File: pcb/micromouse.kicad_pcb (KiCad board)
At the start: 2 copper layers, 46 x 84 mm, 64 parts, among them J1 PINHD_1x6_Female, J10 B2B-PH-K-S, J11 B2B-PH-K-S, J12 PINHD_1x5_Female, J13 B6B-ZR, J14 PINHD_1x8_Male, J15 PINHD_1x6_Male, J16 PINHD_1x2_Male, J2 PINHD_1x6_Female, J3 PINHD_1x4_Female, J4 PINHD_1x6_Female, J5 PINHD_1x4_Female, J6 PINHD_1x6_Female, J7 PINHD_1x8_Female, J8 PINHD_1x2_Female, J9 B6B-ZR, M1 Left, M2 Right, SW1 EG1218, SW2 SW_DIP_x04, SW3 Push_Button, U1 STM32F411RETx, U2 ICM-42688-P, U3 L293DD, U4 AZ1117-3.3, Y1 32.768 kHz 7 pF, Y2 25 MHz 10 pF

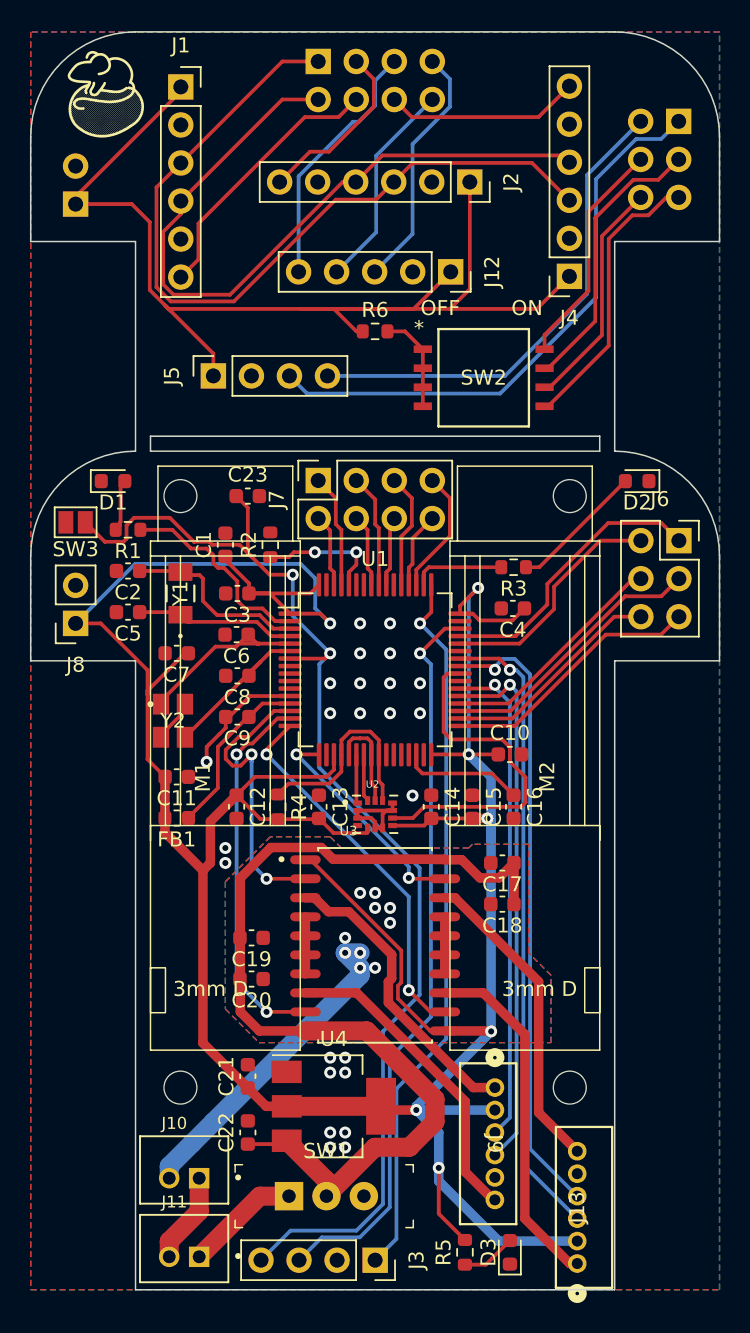
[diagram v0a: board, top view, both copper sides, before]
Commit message: Updated board from MM lead feedback
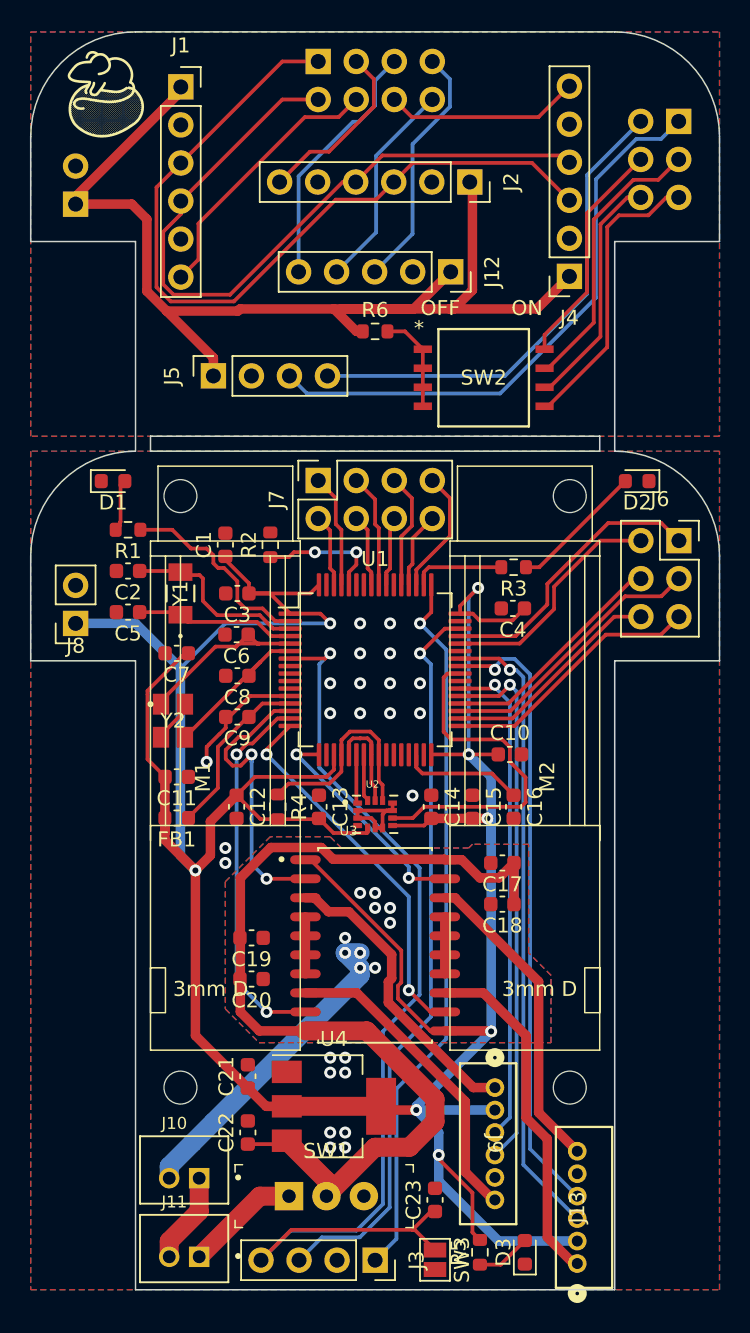
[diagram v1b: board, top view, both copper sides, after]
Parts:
- moved SW3 54.8 mm to (151.0, 139.0), turned to -90 degrees
- moved C23 48.6 mm to (151.0, 135.0), turned to 90 degrees
- moved D3 1.00 mm to (157.0, 138.5)
- moved R5 1.00 mm to (154.0, 138.5)
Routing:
- net NRST: track 81.3 -> 68.4 mm, vias 2 -> 1
- net +3.3V: track 215.6 -> 225.3 mm, vias 7 -> 8
- net /Breakout Board/+3.3V: track 80.5 -> 77.0 mm
- net /Breakout Board/DEBUG2: track 15.5 -> 16.1 mm
- net /Breakout Board/DEBUG1: track 18.9 -> 19.4 mm
